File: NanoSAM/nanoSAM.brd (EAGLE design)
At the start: 95.9 x 90.2 mm, 91 parts, among them IC3 AD5241, J1 POWER_JACK, U1 LTC3260EMSEPBF

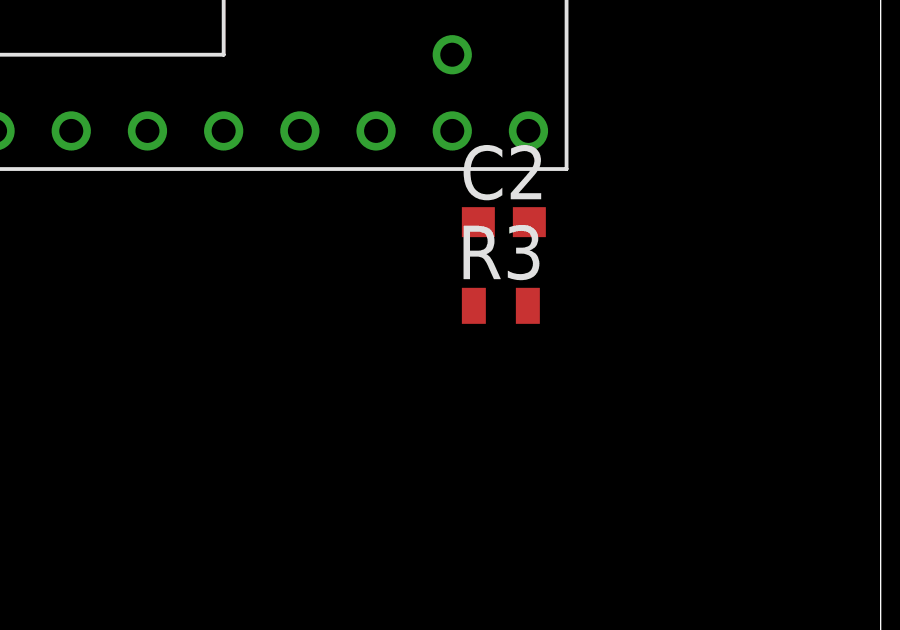
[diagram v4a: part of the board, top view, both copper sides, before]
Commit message: added power plane
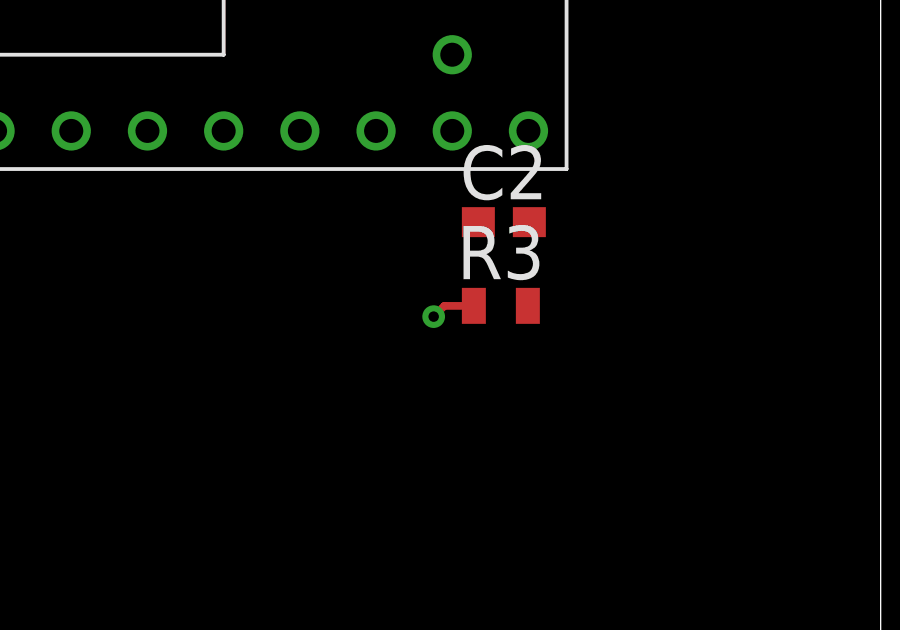
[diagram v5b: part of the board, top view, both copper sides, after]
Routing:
- net +3V3: track 0.00 -> 1.49 mm, vias 0 -> 1
- added copper zone on layer 15, net +3.3V
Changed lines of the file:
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@@
 <?xml version="1.0" encoding="utf-8"?>
 <!DOCTYPE eagle SYSTEM "eagle.dtd">
-<eagle version="9.5.1">
+<eagle version="9.3.0">
 <drawing>
 <settings>
@@
 <layers>
 <layer number="1" name="Top" color="4" fill="1" visible="yes" active="yes"/>
-<layer number="2" name="Route2" color="16" fill="1" visible="no" active="yes"/>
+<layer number="2" name="Route2" color="16" fill="1" visible="yes" active="yes"/>
 <layer number="3" name="Route3" color="17" fill="1" visible="no" active="no"/>
 <layer number="4" name="Route4" color="18" fill="1" visible="no" active="no"/>
@@
 <wire x1="-52.49" y1="63.5" x2="-48.26" y2="54.61" width="0" layer="19" extent="1-1"/>
 <wire x1="-22.01" y1="67.31" x2="-48.26" y2="54.61" width="0" layer="19" extent="1-1"/>
-<wire x1="15.3" y1="68.1" x2="-22.01" y2="67.31" width="0" layer="19" extent="1-1"/>
+<wire x1="15.275" y1="68.125" x2="-22.01" y2="67.31" width="0" layer="19" extent="1-1"/>
 <wire x1="19.7744" y1="16.08866875" x2="15.4056" y2="16.08866875" width="0" layer="19" extent="1-1"/>
 <wire x1="19.7744" y1="18.59056875" x2="19.7744" y2="16.08866875" width="0" layer="19" extent="1-1"/>
@@
 </polygon>
 <wire x1="-95.67" y1="-31.75" x2="-113" y2="-72" width="0" layer="19" extent="1-1"/>
-<wire x1="84.19" y1="34.15" x2="-95.67" y2="-31.75" width="0" layer="19" extent="1-1"/>
-<wire x1="-56.3" y1="59.69" x2="84.19" y2="34.15" width="0" layer="19" extent="1-1"/>
+<wire x1="-56.3" y1="59.69" x2="-95.67" y2="-31.75" width="0" layer="19" extent="1-1"/>
 <wire x1="-52.49" y1="59.69" x2="-56.3" y2="59.69" width="0" layer="19" extent="1-1"/>
 <wire x1="-56.3" y1="63.5" x2="-56.3" y2="59.69" width="0" layer="19" extent="1-1"/>
@@
 <wire x1="67.73" y1="71.925" x2="71" y2="86" width="0" layer="19" extent="1-1"/>
 <wire x1="67.87" y1="63.925" x2="67.73" y2="71.925" width="0" layer="19" extent="1-1"/>
-<wire x1="74.098" y1="15.768" x2="39.48" y2="23.22" width="0" layer="19" extent="1-1"/>
+<wire x1="84.19" y1="34.15" x2="84.16" y2="52.43" width="0" layer="19" extent="1-1"/>
+<wire x1="74.098" y1="15.768" x2="84.19" y2="34.15" width="0" layer="19" extent="1-1"/>
 <wire x1="76.13" y1="13.99" x2="74.098" y2="15.768" width="0" layer="19" extent="1-1"/>
 <wire x1="74.098" y1="12.268" x2="76.13" y2="13.99" width="0" layer="19" extent="1-1"/>
@@
 <contactref element="R35" pad="2"/>
 <contactref element="R36" pad="2"/>
+<wire x1="82.34" y1="31.36" x2="81.36" y2="31.36" width="0.254" layer="1"/>
+<wire x1="81.36" y1="31.36" x2="81" y2="31" width="0.254" layer="1"/>
+<via x="81" y="31" extent="1-16" drill="0.35"/>
 <wire x1="-114.6" y1="-108" x2="-114.6" y2="-117" width="0" layer="19" extent="1-1"/>
 <wire x1="-114.6" y1="-99" x2="-114.6" y2="-108" width="0" layer="19" extent="1-1"/>
@@
 <wire x1="-114.6" y1="-89" x2="-114.6" y2="-94" width="0" layer="19" extent="1-1"/>
 <wire x1="-88.53" y1="-10.16" x2="-114.6" y2="-89" width="0" layer="19" extent="1-1"/>
-<wire x1="82.34" y1="31.36" x2="-88.53" y2="-10.16" width="0" layer="19" extent="1-1"/>
-<wire x1="-68.21" y1="54.61" x2="82.34" y2="31.36" width="0" layer="19" extent="1-1"/>
+<wire x1="-68.21" y1="54.61" x2="-88.53" y2="-10.16" width="0" layer="19" extent="1-1"/>
 <wire x1="-64.4" y1="54.61" x2="-68.21" y2="54.61" width="0" layer="19" extent="1-1"/>
 <wire x1="-51.17" y1="54.61" x2="-64.4" y2="54.61" width="0" layer="19" extent="1-1"/>
@@
 <wire x1="-25.82" y1="67.31" x2="-31.33" y2="59.69" width="0" layer="19" extent="1-1"/>
 <wire x1="32.89" y1="72.4" x2="-18.105" y2="47.48" width="0" layer="19" extent="1-1"/>
+<wire x1="81" y1="31" x2="32.89" y2="72.4" width="0" layer="19" extent="1-1"/>
 </signal>
 <signal name="VBUS">
@@
 <contactref element="U$2" pad="3.3V@2"/>
 <contactref element="U$2" pad="3.3V@1"/>
+<wire x1="82.49" y1="34.15" x2="84.14" y2="31.36" width="0" layer="19" extent="1-1"/>
+<wire x1="79.08" y1="37.19" x2="82.49" y2="34.15" width="0" layer="19" extent="1-1"/>
 <wire x1="51.14" y1="39.73" x2="79.08" y2="37.19" width="0" layer="19" extent="1-1"/>
 <wire x1="51.14" y1="47.35" x2="51.14" y2="39.73" width="0" layer="19" extent="1-1"/>
-<wire x1="84.14" y1="31.36" x2="51.14" y2="39.73" width="0" layer="19" extent="1-1"/>
-<wire x1="82.49" y1="34.15" x2="84.14" y2="31.36" width="0" layer="19" extent="1-1"/>
 </signal>
 <signal name="FLASH_CS1">
@@
 <wire x1="80.54" y1="86" x2="68.92" y2="37.19" width="0" layer="19" extent="1-1"/>
 </signal>
+<signal name="+3.3V">
+<polygon width="0.1524" layer="15">
+<vertex x="36" y="90"/>
+<vertex x="36" y="0"/>
+<vertex x="96" y="0"/>
+<vertex x="96" y="90"/>
+</polygon>
+</signal>
 </signals>

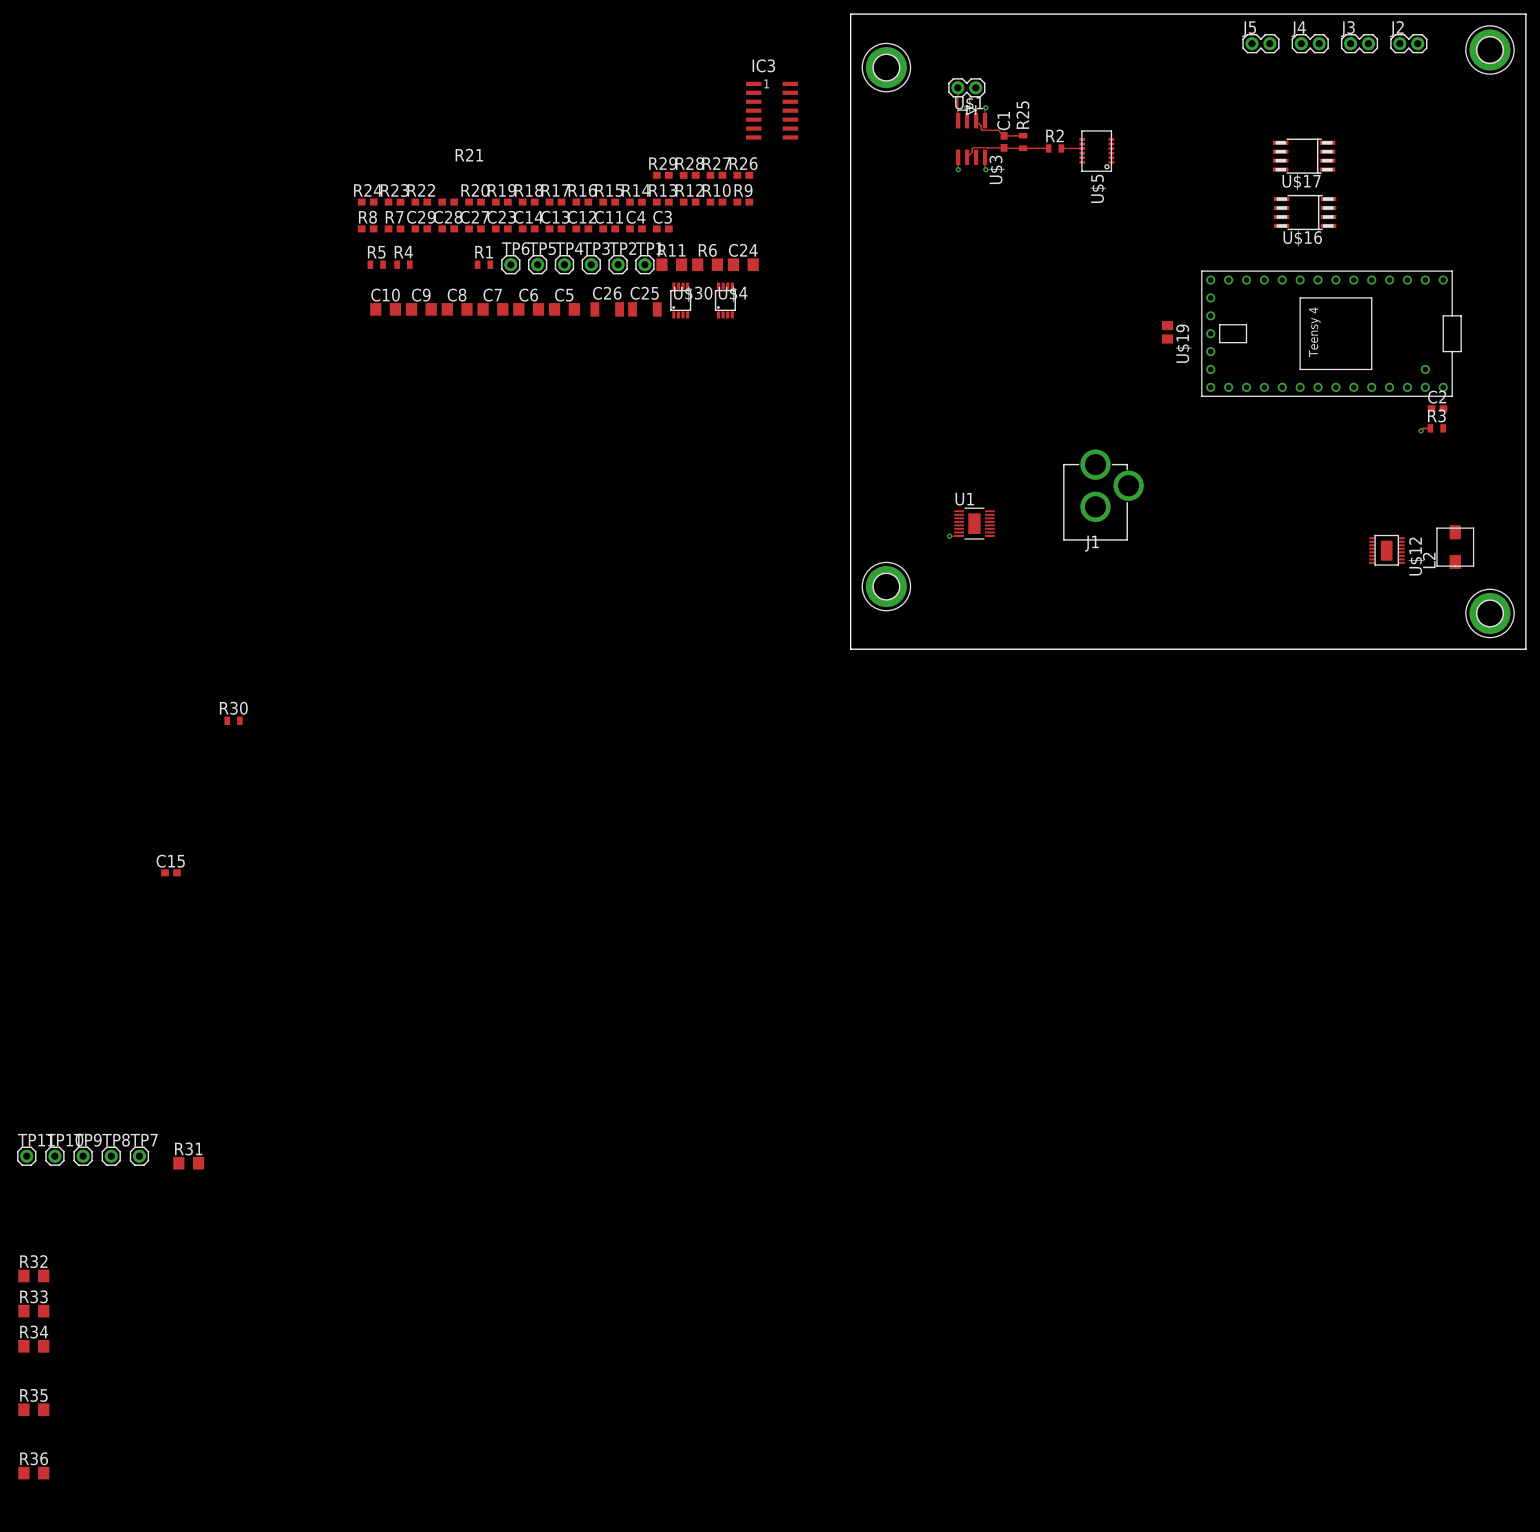
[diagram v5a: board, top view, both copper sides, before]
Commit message: Added R4, R30, C15, C14 to flash.
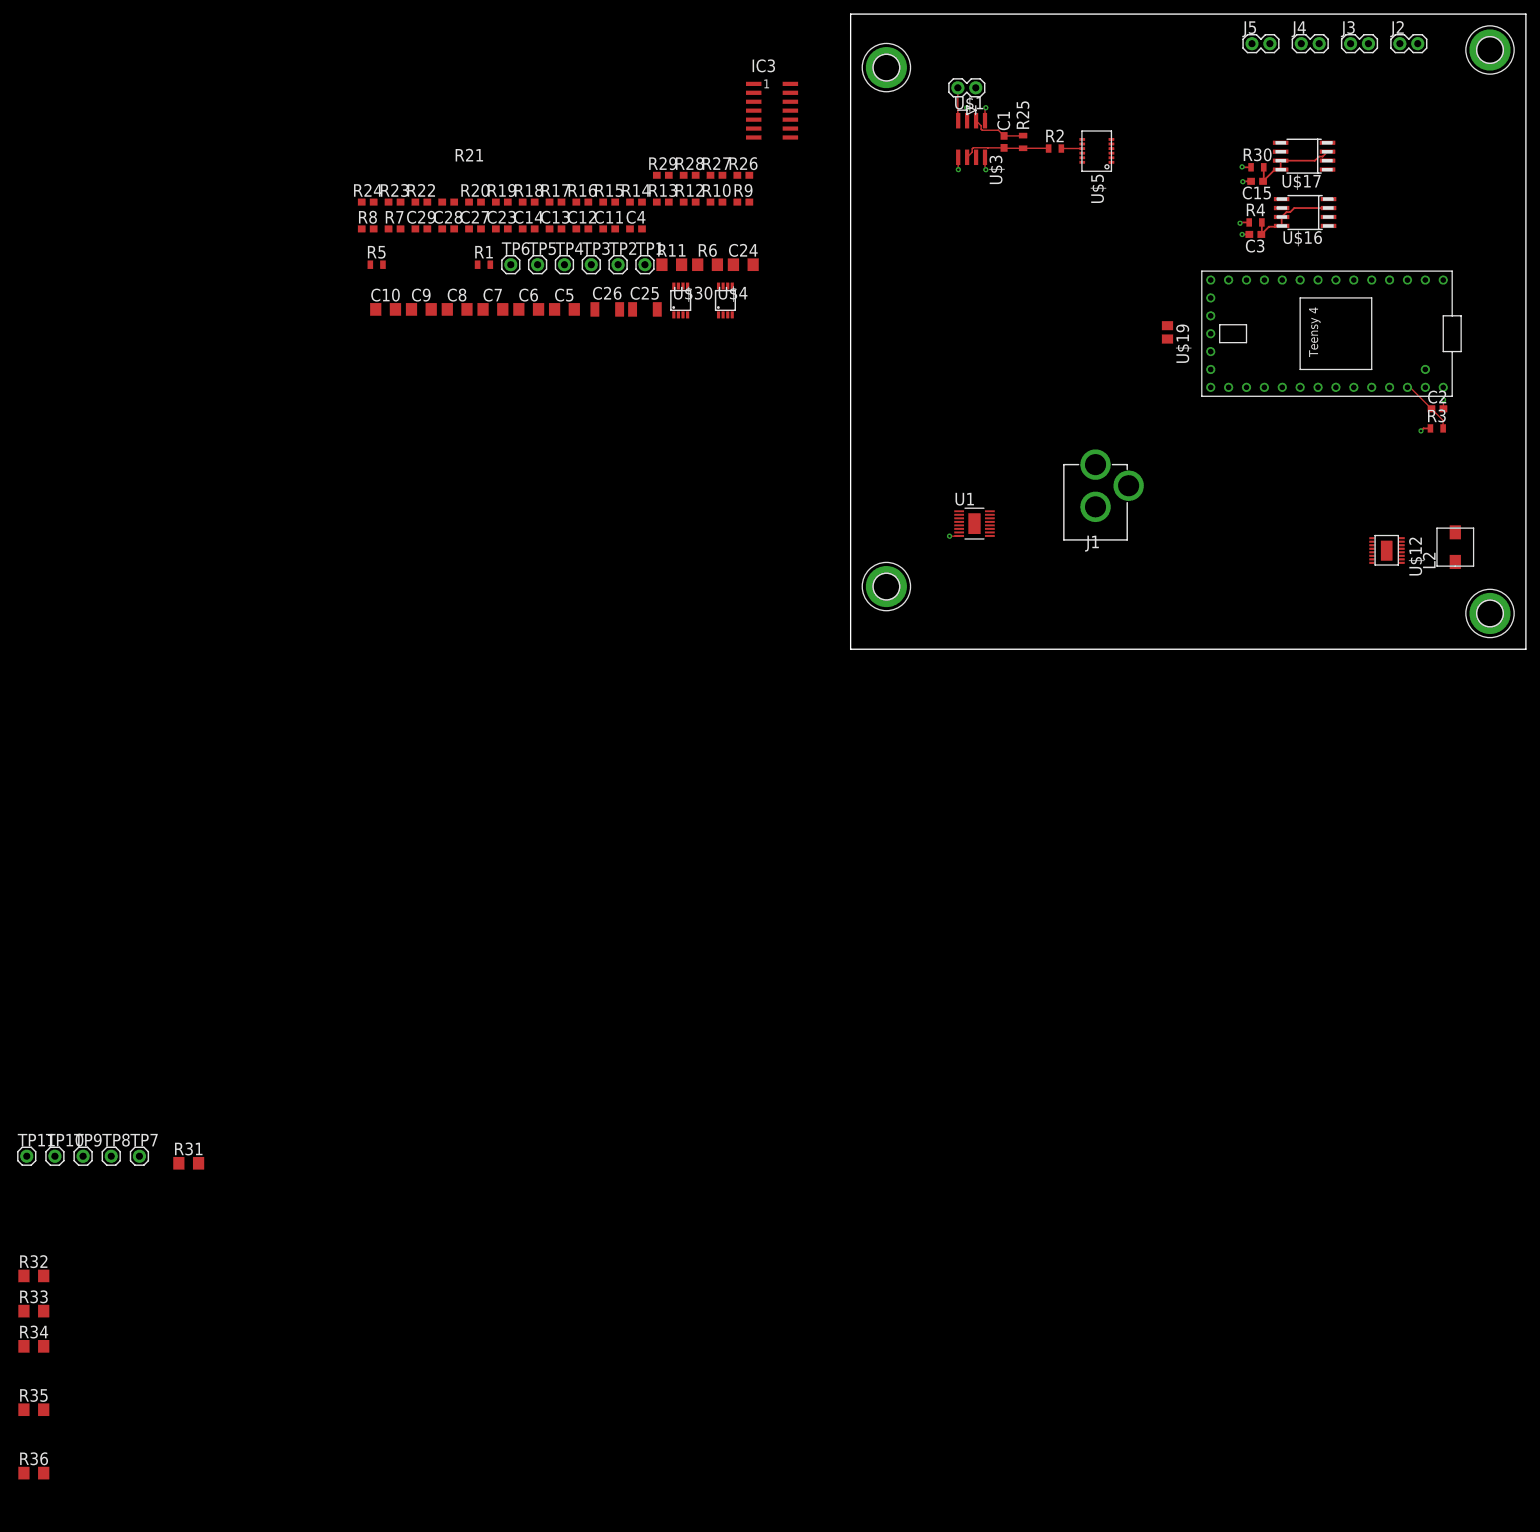
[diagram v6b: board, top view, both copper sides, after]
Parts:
- moved C15 182.8 mm to (57.7, 66.5), turned to 180 degrees
- moved R30 165.3 mm to (57.8, 68.4)
- moved R4 121.1 mm to (57.5, 60.6)
- moved C3 84.1 mm to (57.5, 58.9), turned to 180 degrees
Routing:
- net N$29: track 0.00 -> 13.7 mm
- net N$8: track 0.00 -> 13.6 mm
- net N$4: track 0.00 -> 8.14 mm
- net DGND: track 0.00 -> 3.47 mm, vias 0 -> 3
- net +3V3: track 1.49 -> 4.13 mm, vias 1 -> 3

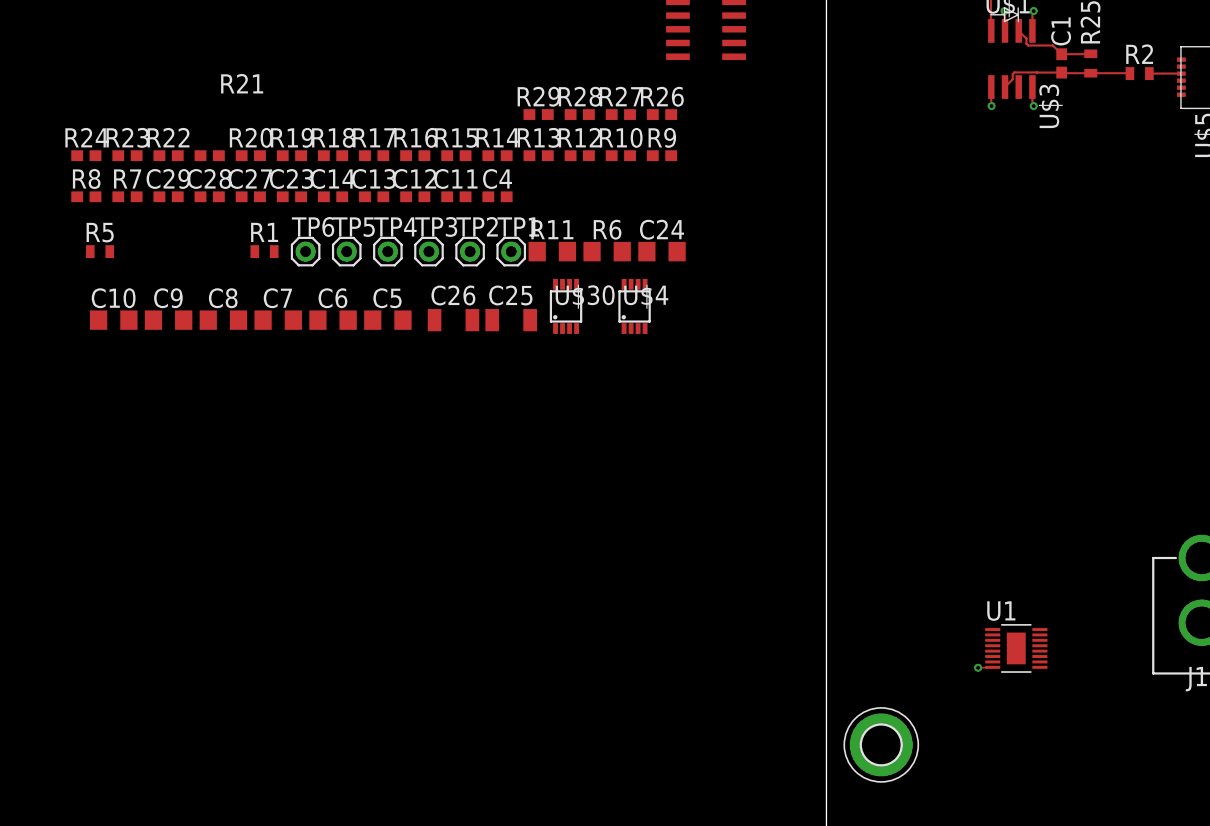
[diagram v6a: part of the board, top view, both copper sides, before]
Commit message: moved some resistors around
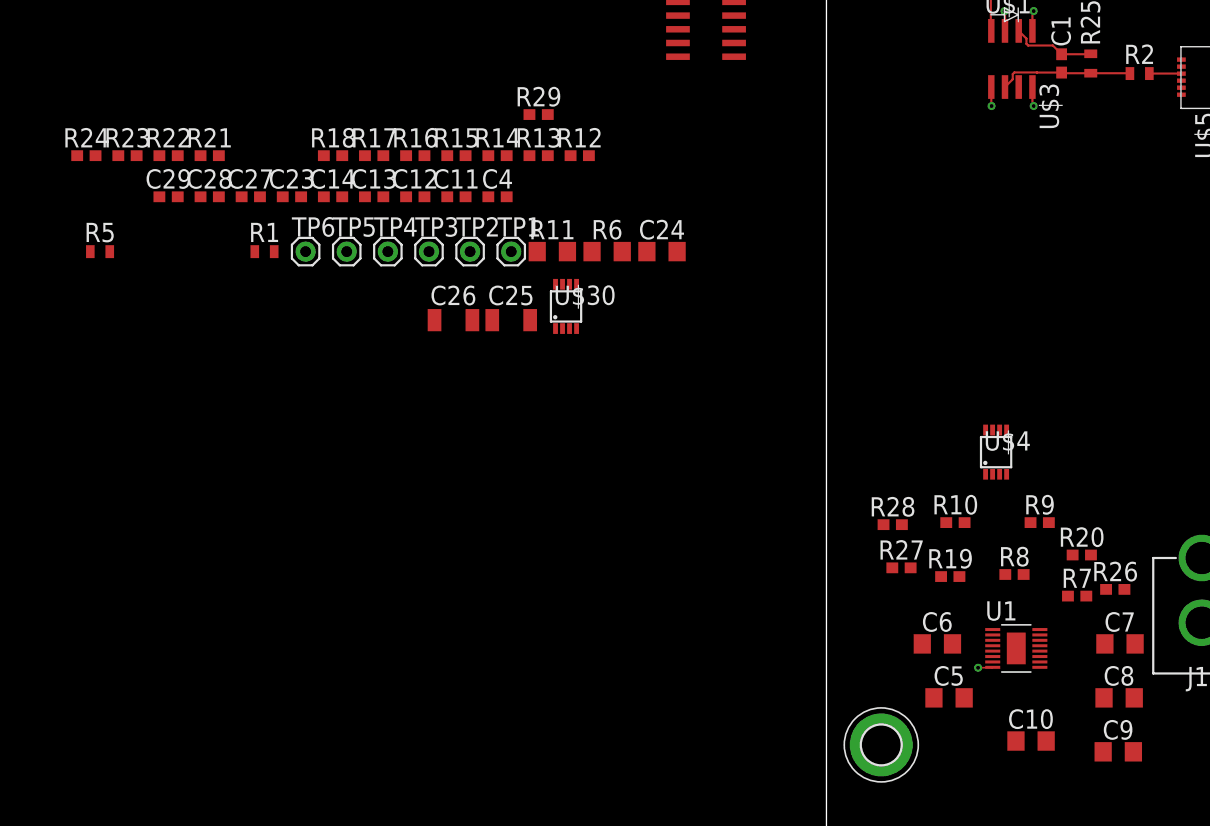
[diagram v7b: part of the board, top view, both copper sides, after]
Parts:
- moved C9 96.7 mm to (27.0, 8.26)
- moved R7 95.5 mm to (23.2, 22.7)
- moved C10 93.5 mm to (19.0, 9.26)
- moved R8 92.8 mm to (17.4, 24.7)
- moved C8 90.1 mm to (27.1, 13.3)
- moved R20 85.4 mm to (23.7, 26.5)
- moved C7 83.6 mm to (27.2, 18.3)
- moved R19 72.4 mm to (11.5, 24.5)
- moved C6 63.5 mm to (10.3, 18.3)
- moved C5 62.7 mm to (11.4, 13.3)
- moved R26 60.8 mm to (26.8, 23.3)
- moved R27 49.4 mm to (6.95, 25.3)
- moved R9 48.8 mm to (19.8, 29.5)
- moved R28 47.8 mm to (6.14, 29.3)
- moved R10 46.0 mm to (11.9, 29.5)
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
